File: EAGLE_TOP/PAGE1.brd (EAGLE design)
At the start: 160 x 160 mm, 101 parts, among them Q1 IRF640, U1 NE555_SOP8, U10 NE556_SOP14, U11 4017_SOP16, U12 4017_SOP16, U13 4518_SMD, U14 4510_DIP, U15 4001_SOP14, U16 4081, U2 4040, U3 4030, U4 4030, U5 LM324, U6 4081_SMD, U7 4017_SOP16, U8 4013_SMD, U9 4013_SMD

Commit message: top PCB completed
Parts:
- removed C11, C15, C16, C19, C2, C20, C21, C22, C23, C24, C25, C26, C27, C5, C6, C7, C8, C9: 0.1uF, !JKS:SMD2012
- removed C12, C13, C14, C17, C18, C3: 10uF, !JKS:CAP_POL
- removed C4: 0.012uF, !JKS:CAP_POL
- removed D1, D10, D11, D12, D13, D14, D15, D16, D2, D3, D4, D5, D6, D7, D8, D9: 1N4148, !JKS:SMD_DIODE
- removed LED1, LED2, LED3, LED4: (no value), !JKS:LED_5MM_BEN
- removed P1: (no value), !JKS:POWER_2
- removed R11, R12, R14, R15, R39, R41, R43, R45, R46, R47: 20K, !JKS:SMD2012
- removed R13, R16, R34, R36, R38, R40, R42, R44, R48: 10K, !JKS:SMD2012
- removed R18: 1K, !JKS:SMD2012
- removed R19, R20, R21: 100k, !JKS:SMD2012
- removed R35, R37: 2.2K, !JKS:SMD2012
- removed U1: NE555_SOP8, !JKS:SOP8
- removed U10: NE556_SOP14, !JKS:SOP14
- removed U11, U12, U7: 4017_SOP16, !JKS:SOP16
- removed U13: 4518_SMD, !JKS:SOP16
- removed U14: 4510_DIP, !JKS:DIP16
- removed U15: 4001_SOP14, !JKS:SOP14
- removed U16: 4081, !JKS:DIP14
- removed U2: 4040, !JKS:DIP16
- removed U3, U4: 4030, !JKS:DIP14
- removed U5: LM324, !JKS:DIP14
- removed U6: 4081_SMD, !JKS:SOP14
- removed U8, U9: 4013_SMD, !SEM_03:SOIC_14
- removed VR1: 10K, !JKS:3RP/1610N
- added CON1: TREE_CON, !JKS:TREE_CON
- added Q2, Q3: C1815, !JKS:TO92
- added Q4, Q5, Q6: IRF640, transistor-fet:TO220
- added SW1: (no value), !JKS:PUSH_SW
- C1: value 0.1uF -> 47pF; device !JKS:CAP_POL -> !JKS:SMD2012
- Q1: value IRF640 -> C1815; device transistor-fet:TO220 -> !JKS:TO92
- R10, R8: value 10K -> 1K
- R2: value 1K -> 470k
- R3: value 20K -> 470k
- R4: value 10K -> 470k
- R5: value 20K -> 330
- R6: value 10K -> 220
- R7: value 20K -> 220
- R9: value 20K -> 1K
- moved R4 99.0 mm to (55.9, 118.1), turned to 270 degrees
- moved R3 94.7 mm to (61.0, 113.0), turned to 270 degrees
- moved R7 77.6 mm to (52.1, 91.4)
- moved R6 74.5 mm to (58.4, 91.4), turned to 90 degrees
- moved R5 73.9 mm to (71.6, 99.9), turned to 0 degrees
- moved R2 61.1 mm to (66.0, 108.0), turned to 270 degrees
- moved Q1 57.4 mm to (62.2, 99.1), turned to 315 degrees
- moved R10 57.0 mm to (90.2, 100.3), turned to 180 degrees
- moved R9 40.9 mm to (73.7, 67.3), turned to 0 degrees
- moved R8 28.8 mm to (94.0, 68.6), turned to 180 degrees
- moved R1 20.8 mm to (79.5, 22.9), turned to 0 degrees
- moved C1 20.0 mm to (77.5, 19.1), flipped to the bottom, turned to 180 degrees
- moved IDC1 1.32 mm to (90.4, 148.1)
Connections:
- removed net FASTER_CV: R44.2, R45.2, R47.2, U10.11
- removed net MOD_BREATH: IDC1.10, LED1.1, U6.1, U7.3
- removed net MOD_FAST3: IDC1.12, LED2.1, U15.1, U15.2, U7.2
- removed net MOD_FASTER: C20.1, IDC1.14, LED3.1, U15.8, U15.9, U7.4
- removed net MOD_STATIC: D10.1, D11.1, D9.1, IDC1.16, LED4.1, U7.7
- removed net N$1: D1.1, VR1.1
- removed net N$10: U2.12, U3.8
- removed net N$11: U2.14, U3.12
- removed net N$12: U2.15, U4.1
- removed net N$14: R3.1, U3.3
- removed net N$15: R5.1, U3.4
- removed net N$16: R7.1, U3.10
- removed net N$17: R9.1, U3.11
- removed net N$18: R11.1, U4.3
- removed net N$19: R12.1, R3.2, R4.1
- removed net N$2: R1.2, U1.7, VR1.2
- removed net N$20: R4.2, R5.2, R6.1
- removed net N$21: R6.2, R7.2, R8.1
- removed net N$22: R10.1, R8.2, R9.2
- removed net N$23: R10.2, R11.2, R13.1
- removed net N$24: C3.1, R13.2, U5.3
- removed net N$25: R14.1, U5.1, U5.2
- removed net N$26: R15.2, R16.2, U5.7, U6.2
- removed net N$27: R14.2, R15.1, U5.5
- removed net N$28: C4.1, R16.1, U5.6
- removed net N$29: D3.1, D4.1, D5.1, U6.3
- removed net N$3: D2.2, VR1.3
- removed net N$32: U7.10, U7.15
- removed net N$33: LED1.2, LED2.2, LED3.2, LED4.2, R18.1
- removed net N$34: U6.5, U8.2
- removed net N$35: U6.6, U8.12
- removed net N$36: U6.4, U8.5
- removed net N$37: R19.1, U8.1, U8.9
- removed net N$38: R20.1, U8.13, U9.5
- removed net N$39: U2.1, U3.13, U3.2, U3.6, U3.9, U4.2, U8.11, U8.3, U9.3
- removed net N$4: C2.1, U1.5
- removed net N$40: R21.1, U9.1
- removed net N$5: C1.1, D1.2, D2.1, U1.2, U1.6
- removed net N$58: C17.1, R35.2, U10.2, U10.6
- removed net N$59: R34.2, R35.1, U10.1
- removed net N$6: R2.1, U1.3, U2.10
- removed net N$60: U10.5, U11.14
- removed net N$61: C19.1, U10.3
- removed net N$62: U13.5, U13.7
- removed net N$63: U11.12, U13.2
- removed net N$64: U11.15, U15.3
- removed net N$65: U13.3, U15.5
- removed net N$66: U13.4, U15.6
- removed net N$67: U11.2, U16.1
- removed net N$68: U11.4, U16.5
- removed net N$69: U11.7, U16.8
- removed net N$7: Q1.1, R2.2
- removed net N$70: U15.4, U16.2, U16.6, U16.9
- removed net N$71: D6.1, U16.3
- removed net N$72: D7.1, U16.4
- removed net N$73: D8.1, U16.10
- removed net N$74: R36.2, R37.1, U10.13
- removed net N$75: C18.1, R37.2, U10.12, U10.8
- removed net N$76: C20.2, R48.1, U14.1
- removed net N$77: U10.9, U12.14
- removed net N$78: D12.2, D13.2, U12.15
- removed net N$79: R39.1, U14.6
- removed net N$8: U2.4, U3.1
- removed net N$80: D12.1, U15.10
- removed net N$81: D14.1, U12.2
- removed net N$82: D15.1, U12.4
- removed net N$83: D16.1, U12.7
- removed net N$84: C25.1, D13.1, R38.1
- removed net N$85: U13.13, U13.15
- removed net N$86: R38.2, U12.10, U13.9
- removed net N$87: R41.1, U14.11
- removed net N$88: R43.1, U14.14
- removed net N$89: U13.12, U14.15
- removed net N$9: U2.13, U3.5
- removed net N$90: R45.1, U14.2
- removed net N$91: R39.2, R40.1, R46.1
- removed net N$92: R40.2, R41.2, R42.1
- removed net N$93: R42.2, R43.2, R44.1
- new net LED_ARR1: CON1.5, Q4.2
- new net LED_ARR2: CON1.6, Q5.2
- new net LED_ARR3: CON1.7, Q6.2
- new net N$13: Q4.1, R8.2
- new net N$43: Q5.1, R9.2
- new net N$46: Q6.1, R10.2
- new net N$50: Q1.3, R2.2
- new net N$53: Q2.3, R3.2
- new net N$54: Q3.3, R4.2
- new net N$55: Q1.2, R5.2
- new net N$56: Q2.2, R6.2
- new net N$57: Q3.2, R7.2
- new net RGB_B: CON1.4, R7.1
- new net RGB_G: CON1.3, R6.1
- new net RGB_R: CON1.2, R5.1
- net +5V: now also CON1.1; no longer C11.1, C15.1, C16.1, C21.1, C22.1, C23.1, C24.1, C26.1, C27.1, C5.1, C6.1, C7.1, C8.1, C9.1, P1.1, R34.1, R36.1, R47.1, U1.4, U1.8, U10.10, U10.14, U10.4, U11.16, U12.16, U13.10, U13.16, U14.16, U14.3, U14.4, U15.14, U16.14, U2.16, U3.14, U4.14, U5.4, U6.14, U7.16, U8.14, U9.14
- net GND: now also SW1.P$1; no longer C11.2, C12.2, C13.2, C14.2, C15.2, C16.2, C17.2, C18.2, C19.2, C2.2, C21.2, C22.2, C23.2, C24.2, C25.2, C26.2, C27.2, C3.2, C4.2, C5.2, C6.2, C7.2, C8.2, C9.2, P1.2, Q1.3, R12.2, R18.2, R46.2, R48.2, U1.1, U10.7, U11.13, U11.8, U12.13, U12.8, U13.1, U13.8, U14.10, U14.12, U14.13, U14.5, U14.8, U14.9, U15.7, U16.7, U2.11, U2.8, U3.7, U4.7, U5.11, U6.7, U7.13, U7.8, U8.10, U8.4, U8.6, U8.7, U8.8, U9.4, U9.6, U9.7
- net LED_CON_1: now also R8.1; no longer D14.2, D3.2, D6.2, D9.2
- net LED_CON_2: now also R9.1; no longer D10.2, D15.2, D4.2, D7.2
- net LED_CON_3: now also Q5.3, R10.1; no longer D11.2, D16.2, D5.2, D8.2
- net LED_CON_B: now also R4.1; no longer C14.1, R21.2
- net LED_CON_G: now also R3.1; no longer C13.1, R20.2
- net LED_CON_R: now also R2.1; no longer C12.1, R19.2
- net MAIN_BRIGHT: now also Q1.1, Q2.1, Q3.1, Q4.3, Q6.3; no longer Q1.2
- net MOD_SW: now also C1.1, R1.2, SW1.P$2; no longer U7.14
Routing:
- net +5V: track 728.6 -> 257.5 mm, vias 42 -> 0
- net MOD_FASTER: track 318.5 -> 0.00 mm, vias 4 -> 0
- net MOD_FAST3: track 303.3 -> 0.00 mm, vias 4 -> 0
- net N$60: track 264.4 -> 0.00 mm, vias 4 -> 0
- net LED_ARR3: track 0.00 -> 255.6 mm, vias 0 -> 4
- net N$77: track 233.8 -> 0.00 mm, vias 2 -> 0
- net MAIN_BRIGHT: track 53.1 -> 278.1 mm, vias 2 -> 6
- net RGB_G: track 0.00 -> 224.2 mm
- net MOD_BREATH: track 222.4 -> 0.00 mm, vias 4 -> 0
- net LED_CON_3: track 160.3 -> 376.5 mm, vias 4 -> 6
- net N$39: track 209.2 -> 0.00 mm, vias 4 -> 0
- net MOD_STATIC: track 203.3 -> 0.00 mm, vias 6 -> 0
- net N$6: track 201.9 -> 0.00 mm, vias 6 -> 0
- net RGB_B: track 0.00 -> 171.0 mm
- net LED_CON_B: track 211.8 -> 48.6 mm, vias 2 -> 0
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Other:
- board size 160 x 160 mm -> 161.2 x 161.2 mm
- board text added: "Designed by JsKim"
- board text added: "IC Curcuit"
- board text added: "Tree"
- board text removed: "TREE_BOTTOM"

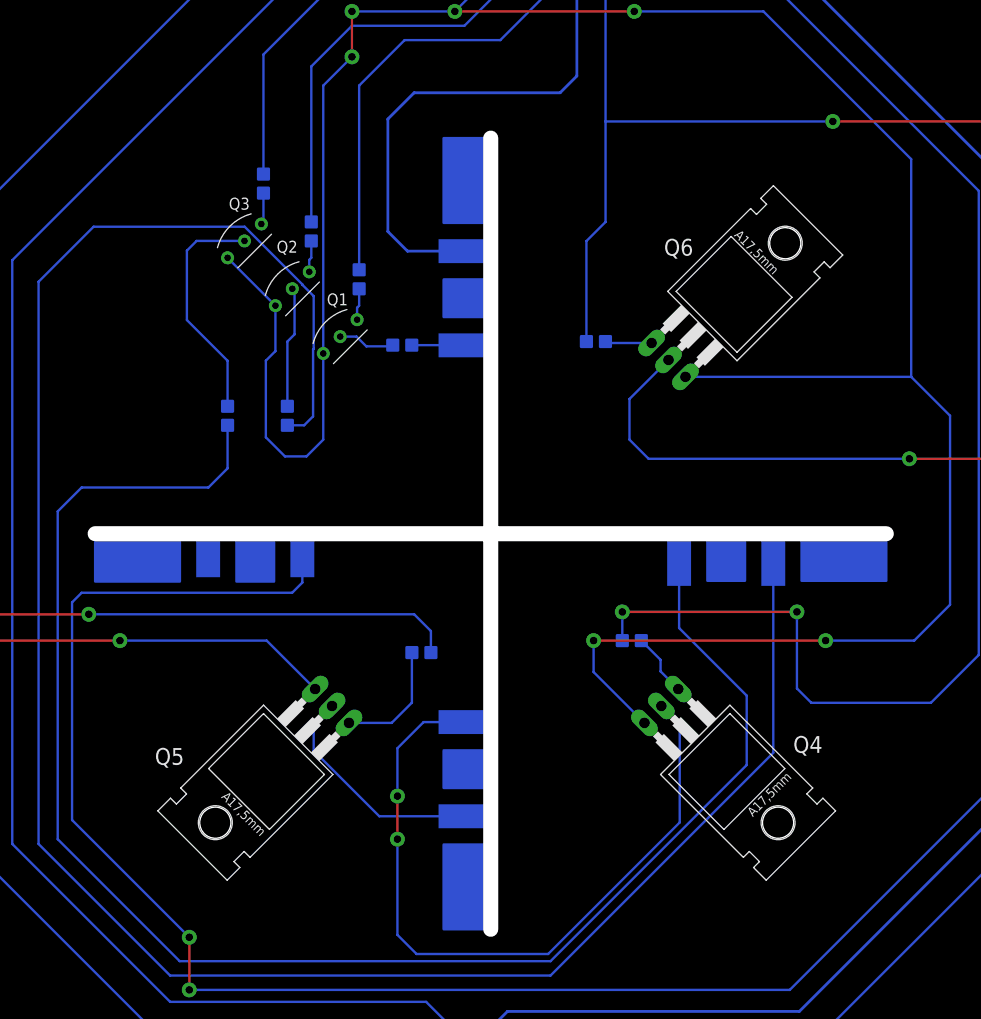
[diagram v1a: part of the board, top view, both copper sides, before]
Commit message: Tree PCB Cmpl, top PCB Mdfi
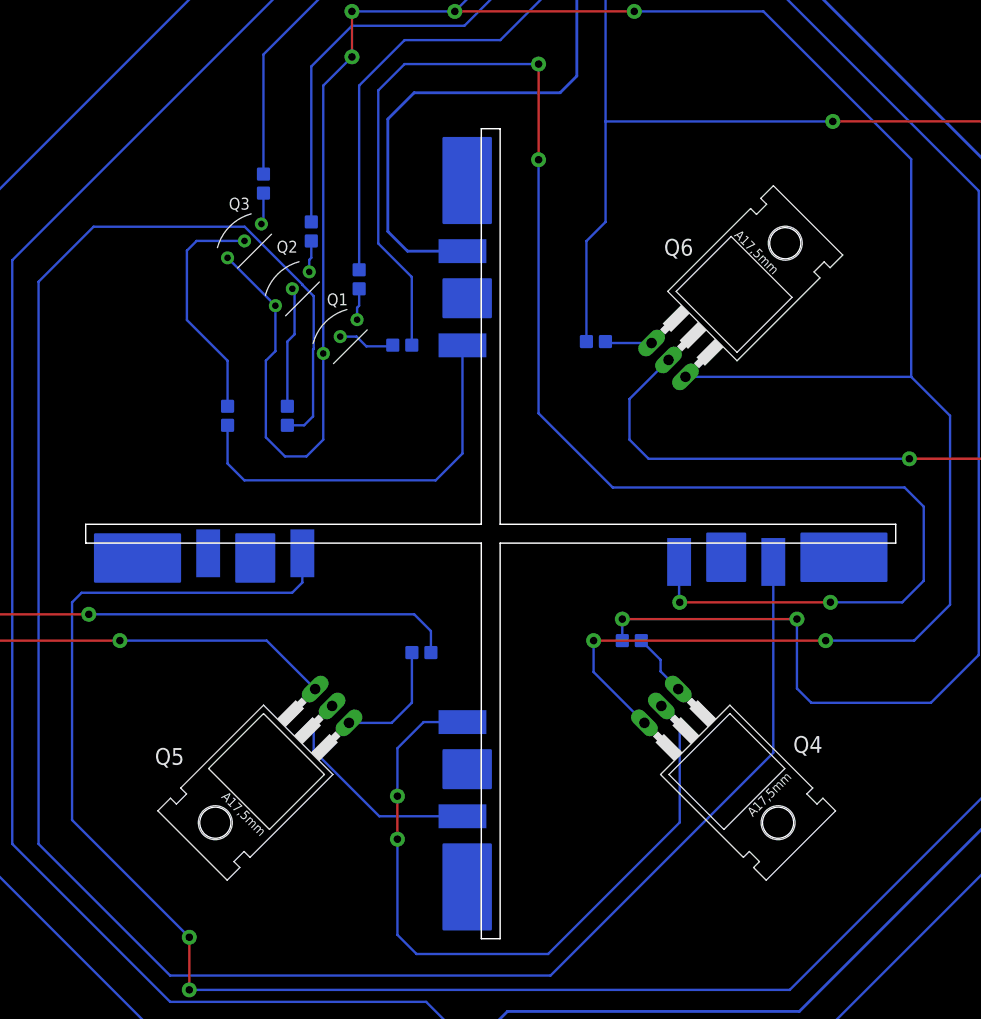
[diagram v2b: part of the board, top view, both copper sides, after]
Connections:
- net RGB_B: now also CON1.2; no longer CON1.4
- net RGB_R: now also CON1.4; no longer CON1.2
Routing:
- net RGB_R: track 5.39 -> 167.8 mm, vias 0 -> 4
- net RGB_B: track 171.0 -> 42.2 mm
- net LED_CON_1: track 154.5 -> 153.0 mm
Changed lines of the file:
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@@
 <setting verticaltext="up"/>
 </settings>
-<grid distance="0.254" unitdist="mm" unit="mm" style="lines" multiple="1" display="yes" altdistance="5" altunitdist="mil" altunit="mil"/>
+<grid distance="0.254" unitdist="mm" unit="mm" style="lines" multiple="1" display="no" altdistance="5" altunitdist="mil" altunit="mil"/>
 <layers>
 <layer number="1" name="Top" color="4" fill="1" visible="yes" active="yes"/>
@@
 <contactref element="R8" pad="1"/>
 <contactref element="IDC1" pad="2"/>
-<wire x1="93.98" y1="68.58" x2="93.98" y2="71.628" width="0.254" layer="16"/>
-<via x="93.98" y="71.628" extent="1-16" drill="0.8" diameter="1.6"/>
-<wire x1="93.98" y1="71.628" x2="112.522" y2="71.628" width="0.254" layer="1"/>
-<via x="112.522" y="71.628" extent="1-16" drill="0.8" diameter="1.6"/>
-<wire x1="112.522" y1="71.628" x2="112.522" y2="63.5" width="0.254" layer="16"/>
+<wire x1="93.98" y1="68.58" x2="93.98" y2="70.866" width="0.254" layer="16"/>
+<via x="93.98" y="70.866" extent="1-16" drill="0.8" diameter="1.6"/>
+<wire x1="93.98" y1="70.866" x2="112.522" y2="70.866" width="0.254" layer="1"/>
+<via x="112.522" y="70.866" extent="1-16" drill="0.8" diameter="1.6"/>
+<wire x1="112.522" y1="70.866" x2="112.522" y2="63.5" width="0.254" layer="16"/>
 <wire x1="112.522" y1="63.5" x2="114.046" y2="61.976" width="0.254" layer="16"/>
 <wire x1="114.046" y1="61.976" x2="126.746" y2="61.976" width="0.254" layer="16"/>
@@
 <signal name="RGB_R">
 <contactref element="R5" pad="1"/>
-<contactref element="CON1" pad="2"/>
-<wire x1="71.628" y1="99.949" x2="76.991" y2="99.949" width="0.254" layer="16"/>
-<wire x1="76.991" y1="99.949" x2="77.01" y2="99.93" width="0.254" layer="16"/>
+<contactref element="CON1" pad="4"/>
+<wire x1="71.628" y1="99.949" x2="71.628" y2="107.188" width="0.254" layer="16"/>
+<wire x1="71.628" y1="107.188" x2="68.072" y2="110.744" width="0.254" layer="16"/>
+<wire x1="68.072" y1="110.744" x2="68.072" y2="127" width="0.254" layer="16"/>
+<wire x1="68.072" y1="127" x2="70.866" y2="129.794" width="0.254" layer="16"/>
+<wire x1="70.866" y1="129.794" x2="85.09" y2="129.794" width="0.254" layer="16"/>
+<via x="85.09" y="129.794" extent="1-16" drill="0.8" diameter="1.6"/>
+<wire x1="85.09" y1="129.794" x2="85.09" y2="119.634" width="0.254" layer="1"/>
+<via x="85.09" y="119.634" extent="1-16" drill="0.8" diameter="1.6"/>
+<wire x1="85.09" y1="119.634" x2="85.09" y2="92.71" width="0.254" layer="16"/>
+<wire x1="85.09" y1="92.71" x2="92.964" y2="84.836" width="0.254" layer="16"/>
+<wire x1="92.964" y1="84.836" x2="123.952" y2="84.836" width="0.254" layer="16"/>
+<wire x1="123.952" y1="84.836" x2="125.984" y2="82.804" width="0.254" layer="16"/>
+<wire x1="125.984" y1="82.804" x2="125.984" y2="74.93" width="0.254" layer="16"/>
+<wire x1="100.01" y1="76.93" x2="100.01" y2="72.71" width="0.254" layer="16"/>
+<wire x1="100.01" y1="72.71" x2="100.076" y2="72.644" width="0.254" layer="16"/>
+<via x="100.076" y="72.644" extent="1-16" drill="0.8" diameter="1.6"/>
+<wire x1="100.076" y1="72.644" x2="116.078" y2="72.644" width="0.254" layer="1"/>
+<via x="116.078" y="72.644" extent="1-16" drill="0.8" diameter="1.6"/>
+<wire x1="116.078" y1="72.644" x2="123.698" y2="72.644" width="0.254" layer="16"/>
+<wire x1="123.698" y1="72.644" x2="125.984" y2="74.93" width="0.254" layer="16"/>
 </signal>
 <signal name="RGB_G">
@@
 <signal name="RGB_B">
 <contactref element="R7" pad="1"/>
-<contactref element="CON1" pad="4"/>
-<wire x1="100.01" y1="76.93" x2="100.01" y2="69.916" width="0.254" layer="16"/>
-<wire x1="100.01" y1="69.916" x2="107.188" y2="62.738" width="0.254" layer="16"/>
-<wire x1="107.188" y1="62.738" x2="107.188" y2="55.372" width="0.254" layer="16"/>
-<wire x1="107.188" y1="55.372" x2="86.36" y2="34.544" width="0.254" layer="16"/>
-<wire x1="86.36" y1="34.544" x2="46.99" y2="34.544" width="0.254" layer="16"/>
-<wire x1="34.036" y1="82.296" x2="36.576" y2="84.836" width="0.254" layer="16"/>
-<wire x1="36.576" y1="84.836" x2="50.038" y2="84.836" width="0.254" layer="16"/>
-<wire x1="50.038" y1="84.836" x2="52.07" y2="86.868" width="0.254" layer="16"/>
-<wire x1="52.07" y1="86.868" x2="52.07" y2="91.44" width="0.254" layer="16"/>
-<wire x1="46.99" y1="34.544" x2="34.036" y2="47.498" width="0.254" layer="16"/>
-<wire x1="34.036" y1="47.498" x2="34.036" y2="82.296" width="0.254" layer="16"/>
+<contactref element="CON1" pad="2"/>
+<wire x1="52.07" y1="91.44" x2="52.07" y2="87.376" width="0.254" layer="16"/>
+<wire x1="52.07" y1="87.376" x2="53.848" y2="85.598" width="0.254" layer="16"/>
+<wire x1="53.848" y1="85.598" x2="74.168" y2="85.598" width="0.254" layer="16"/>
+<wire x1="77.01" y1="88.44" x2="77.01" y2="99.249575" width="0.254" layer="16"/>
+<wire x1="77.01" y1="99.249575" x2="77.3502125" y2="99.5897875" width="0.254" layer="16"/>
+<wire x1="74.168" y1="85.598" x2="77.01" y2="88.44" width="0.254" layer="16"/>
+<wire x1="77.3502125" y1="99.5897875" x2="77.01" y2="99.93" width="0" layer="19" extent="16-16"/>
 </signal>
 </signals>

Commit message: Operation Complete
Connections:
- new net N$1: Q1.1, Q2.1, Q3.1, Q4.3, Q5.3, Q6.3
- net LED_CON_3: no longer Q5.3
- net MAIN_BRIGHT: no longer Q1.1, Q2.1, Q3.1, Q4.3, Q6.3
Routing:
- net MAIN_BRIGHT: track 278.1 -> 179.7 mm
- net N$1: track 0.00 -> 38.4 mm
- net LED_CON_3: track 376.5 -> 369.2 mm
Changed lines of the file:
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@@
 </signal>
 <signal name="MAIN_BRIGHT">
-<contactref element="Q1" pad="1"/>
-<contactref element="Q2" pad="1"/>
-<contactref element="Q3" pad="1"/>
 <contactref element="IDC1" pad="8"/>
-<contactref element="Q4" pad="3"/>
-<contactref element="Q6" pad="3"/>
-<wire x1="62.23" y1="99.06" x2="62.23" y2="89.916" width="0.254" layer="16"/>
-<wire x1="62.23" y1="89.916" x2="60.452" y2="88.138" width="0.254" layer="16"/>
-<wire x1="60.452" y1="88.138" x2="58.166" y2="88.138" width="0.254" layer="16"/>
-<wire x1="58.166" y1="88.138" x2="56.134" y2="90.17" width="0.254" layer="16"/>
-<wire x1="56.134" y1="90.17" x2="56.134" y2="98.298" width="0.254" layer="16"/>
-<wire x1="57.15" y1="99.314" x2="57.15" y2="104.14" width="0.254" layer="16"/>
-<wire x1="56.134" y1="98.298" x2="57.15" y2="99.314" width="0.254" layer="16"/>
-<wire x1="57.15" y1="104.14" x2="52.07" y2="109.22" width="0.254" layer="16"/>
-<wire x1="62.23" y1="99.06" x2="62.23" y2="127.508" width="0.254" layer="16"/>
 <wire x1="62.23" y1="127.508" x2="65.278" y2="130.556" width="0.254" layer="16"/>
 <via x="65.278" y="130.556" extent="1-16" drill="0.8" diameter="1.6"/>
@@
 <wire x1="82.804" y1="141.986" x2="82.804" y2="145.542" width="0.254" layer="16"/>
 <wire x1="76.2" y1="135.382" x2="82.804" y2="141.986" width="0.254" layer="16"/>
-<wire x1="96.32981875" y1="59.844075" x2="90.932" y2="65.24189375" width="0.254" layer="16"/>
 <wire x1="90.932" y1="65.24189375" x2="90.932" y2="68.58" width="0.254" layer="16"/>
 <via x="90.932" y="68.58" extent="1-16" drill="0.8" diameter="1.6"/>
@@
 <wire x1="124.968" y1="68.58" x2="128.778" y2="72.39" width="0.254" layer="16"/>
 <wire x1="128.778" y1="72.39" x2="128.778" y2="92.456" width="0.254" layer="16"/>
-<wire x1="124.65018125" y1="96.58381875" x2="100.683921875" y2="96.58381875" width="0.254" layer="16"/>
 <wire x1="128.778" y1="92.456" x2="124.65018125" y2="96.58381875" width="0.254" layer="16"/>
 <wire x1="124.65018125" y1="96.58381875" x2="124.65018125" y2="119.69781875" width="0.254" layer="16"/>
@@
 <contactref element="R10" pad="1"/>
 <contactref element="IDC1" pad="6"/>
-<contactref element="Q5" pad="3"/>
 <wire x1="85.344" y1="145.542" x2="85.344" y2="139.7" width="0.254" layer="16"/>
 <via x="85.344" y="139.7" extent="1-16" drill="0.8" diameter="1.6"/>
@@
 <wire x1="90.17" y1="100.33" x2="90.17" y2="110.998" width="0.254" layer="16"/>
 <wire x1="90.17" y1="110.998" x2="92.202" y2="113.03" width="0.254" layer="16"/>
-<wire x1="61.368075" y1="63.436178125" x2="56.224253125" y2="68.58" width="0.254" layer="16"/>
 <wire x1="56.224253125" y1="68.58" x2="40.64" y2="68.58" width="0.254" layer="16"/>
 <via x="40.64" y="68.58" extent="1-16" drill="0.8" diameter="1.6"/>
@@
 <wire x1="77.3502125" y1="99.5897875" x2="77.01" y2="99.93" width="0" layer="19" extent="16-16"/>
 </signal>
+<signal name="N$1">
+<contactref element="Q6" pad="3"/>
+<contactref element="Q1" pad="1"/>
+<contactref element="Q2" pad="1"/>
+<contactref element="Q3" pad="1"/>
+<contactref element="Q4" pad="3"/>
+<contactref element="Q5" pad="3"/>
+<wire x1="62.23" y1="99.06" x2="62.23" y2="89.916" width="0.254" layer="16"/>
+<wire x1="62.23" y1="89.916" x2="60.452" y2="88.138" width="0.254" layer="16"/>
+<wire x1="60.452" y1="88.138" x2="58.166" y2="88.138" width="0.254" layer="16"/>
+<wire x1="58.166" y1="88.138" x2="56.134" y2="90.17" width="0.254" layer="16"/>
+<wire x1="56.134" y1="90.17" x2="56.134" y2="98.298" width="0.254" layer="16"/>
+<wire x1="57.15" y1="99.314" x2="57.15" y2="104.14" width="0.254" layer="16"/>
+<wire x1="56.134" y1="98.298" x2="57.15" y2="99.314" width="0.254" layer="16"/>
+<wire x1="57.15" y1="104.14" x2="52.07" y2="109.22" width="0.254" layer="16"/>
+<wire x1="96.32981875" y1="59.844075" x2="100.683921875" y2="96.58381875" width="0" layer="19" extent="1-1"/>
+<wire x1="61.368075" y1="63.436178125" x2="96.32981875" y2="59.844075" width="0" layer="19" extent="1-1"/>
+<wire x1="62.23" y1="99.06" x2="61.368075" y2="63.436178125" width="0" layer="19" extent="1-1"/>
+</signal>
 </signals>

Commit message: ver1 Complete
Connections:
- removed net N$1: Q1.1, Q2.1, Q3.1, Q4.3, Q5.3, Q6.3
- net MAIN_BRIGHT: now also Q1.1, Q2.1, Q3.1, Q4.3, Q5.3, Q6.3
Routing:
- net LED_CON_3: track 369.2 -> 52.9 mm, vias 6 -> 2
- net MAIN_BRIGHT: track 179.7 -> 359.4 mm
- net N$1: track 38.4 -> 0.00 mm
- net RGB_G: track 224.2 -> 237.6 mm
- net LED_ARR3: track 255.6 -> 265.6 mm
- net MOD_SW: track 187.9 -> 197.8 mm
- net RGB_R: track 167.8 -> 175.9 mm
- net RGB_B: track 42.2 -> 39.6 mm
- net LED_CON_B: track 48.6 -> 50.8 mm
- net LED_CON_R: track 55.1 -> 56.9 mm
- net LED_CON_1: track 153.0 -> 154.5 mm
- net LED_CON_G: track 52.1 -> 53.2 mm
- net LED_CON_2: track 178.4 -> 177.5 mm
